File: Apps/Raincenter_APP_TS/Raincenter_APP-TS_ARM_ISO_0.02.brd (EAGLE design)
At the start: 42.3 x 27.4 mm, 26 parts

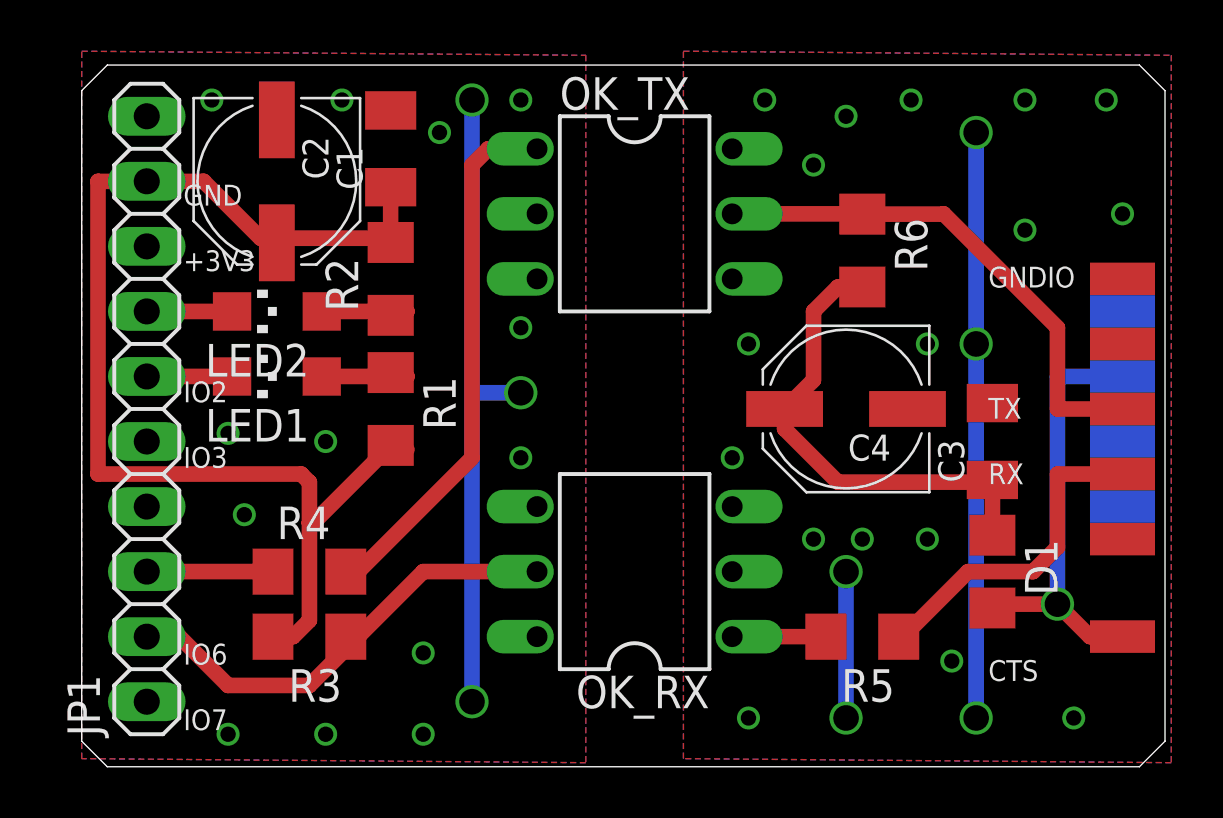
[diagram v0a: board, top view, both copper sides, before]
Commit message: Raincenter App: positioned tNames & bNames for production
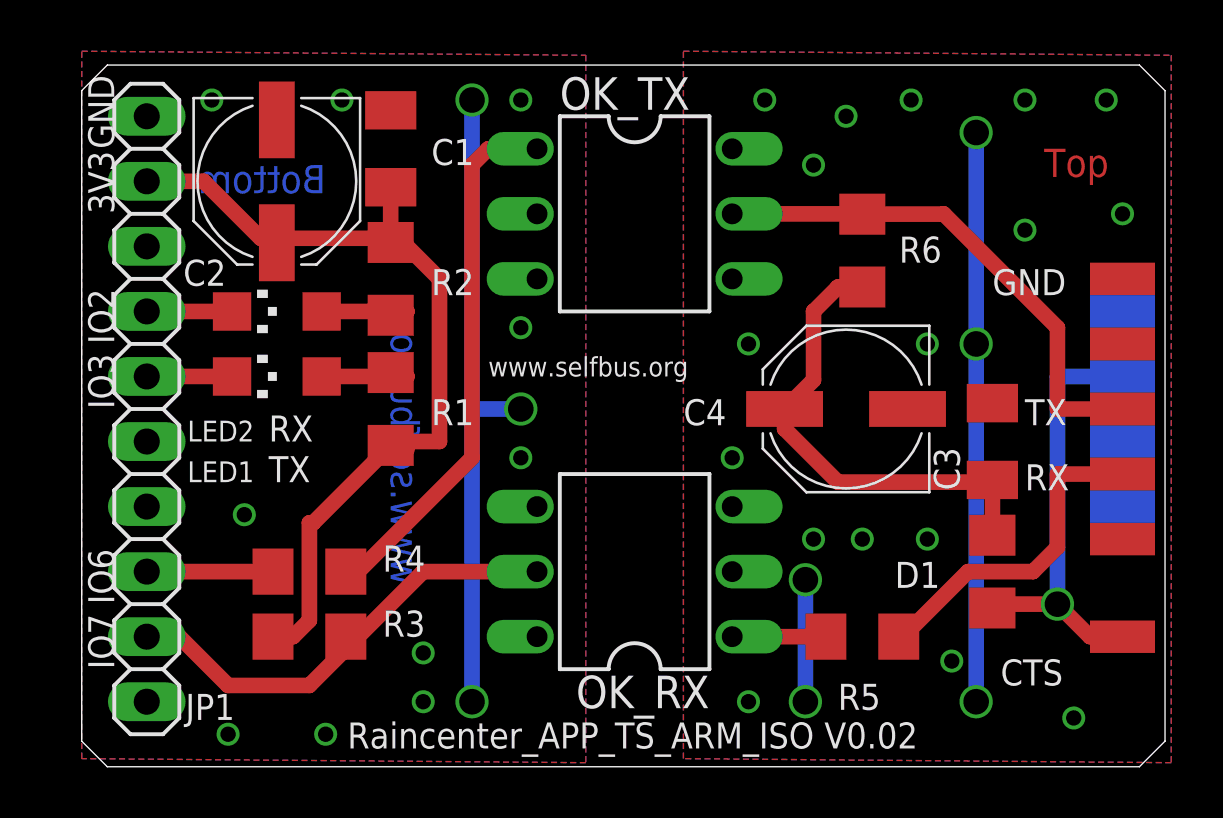
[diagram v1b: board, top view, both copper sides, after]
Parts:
- C2, C4: value 100µF 25V -> 100µF/25V
- LED1: value green -> RX-green
- LED2: value yellow -> TX-yellow
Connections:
- net RX_TX renamed RC_TX
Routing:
- net +3V3: track 47.4 -> 34.9 mm
- net GNDIO: track 28.6 -> 27.0 mm
- net GND: vias 16 -> 13
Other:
- board text added: "3V3"
- board text added: "Bottom"
- board text added: "CTS"
- board text added: "GND"
- board text added: "IO2"
- board text added: "IO3"
- board text added: "IO6"
- board text added: "IO7"
- board text added: "RX"
- board text added: "Raincenter_APP_TS_ARM_ISO V0.02"
- board text added: "TX"
- board text added: "Top"
- board text added: "www.selfbus.org"
- board text removed: "GND +3V3 IO2 IO3 IO6 IO7"
- board text removed: "GNDIO TX RX CTS"
